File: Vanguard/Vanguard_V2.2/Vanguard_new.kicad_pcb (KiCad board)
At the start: 4 copper layers, 50 x 41.2 mm, 73 parts, among them J1 USB_C_Receptacle_USB2.0_16P, J2 Conn_02x03_Pin, J3 Micro_SD_Card_Det1, J4 STARBOARD_SERVO, J5 PORTSIDE_SERVO, J6 Conn_01x02_Pin, Q1 BSS138, Q2 BSS138, Q3 BSS138, Q4 BSS138, U1 ATSAMD11D14A-M, U2 ATmega4809-A, U3 AT25DF641A-SH-T, U4 AP2112K-3.3, U5 BD1020HFV, U6 BNO086, U7 TXB0104D, U8 TPS61092, U9 MPM3610AGQV-P, Y1 32.768kHz

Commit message: forgot a wire
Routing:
- net GND: track 152.7 -> 154.5 mm, vias 22 -> 23

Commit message: more wiring
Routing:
- net Net-(D1-GND): track 34.9 -> 44.5 mm, vias 2 -> 4
- net GND: track 154.5 -> 162.0 mm, vias 23 -> 25
- net Net-(D1-I/O1): track 22.6 -> 25.1 mm
- net Net-(PORTSIDE_RGB1-RA): track 0.00 -> 1.45 mm
- net Net-(D3-A): track 0.00 -> 0.83 mm

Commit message: some drc fixes not done
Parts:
- moved D6 0.66 mm to (528.0, 91.3)
- moved C4 0.40 mm to (526.0, 93.2)
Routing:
- net Net-(D1-GND): track 44.5 -> 45.6 mm
- net Net-(D6-K): track 21.9 -> 21.0 mm
- net GND: track 162.0 -> 161.5 mm

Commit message: Vangaurd 2.2. Done.
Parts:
- added ?: , clipboard:b9f70def-b1a4-4804-8b04-89d3a63594a6, F.Cu at (548.0, 88.5)
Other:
- board text added: "Portside"
- board text added: "Starboard"

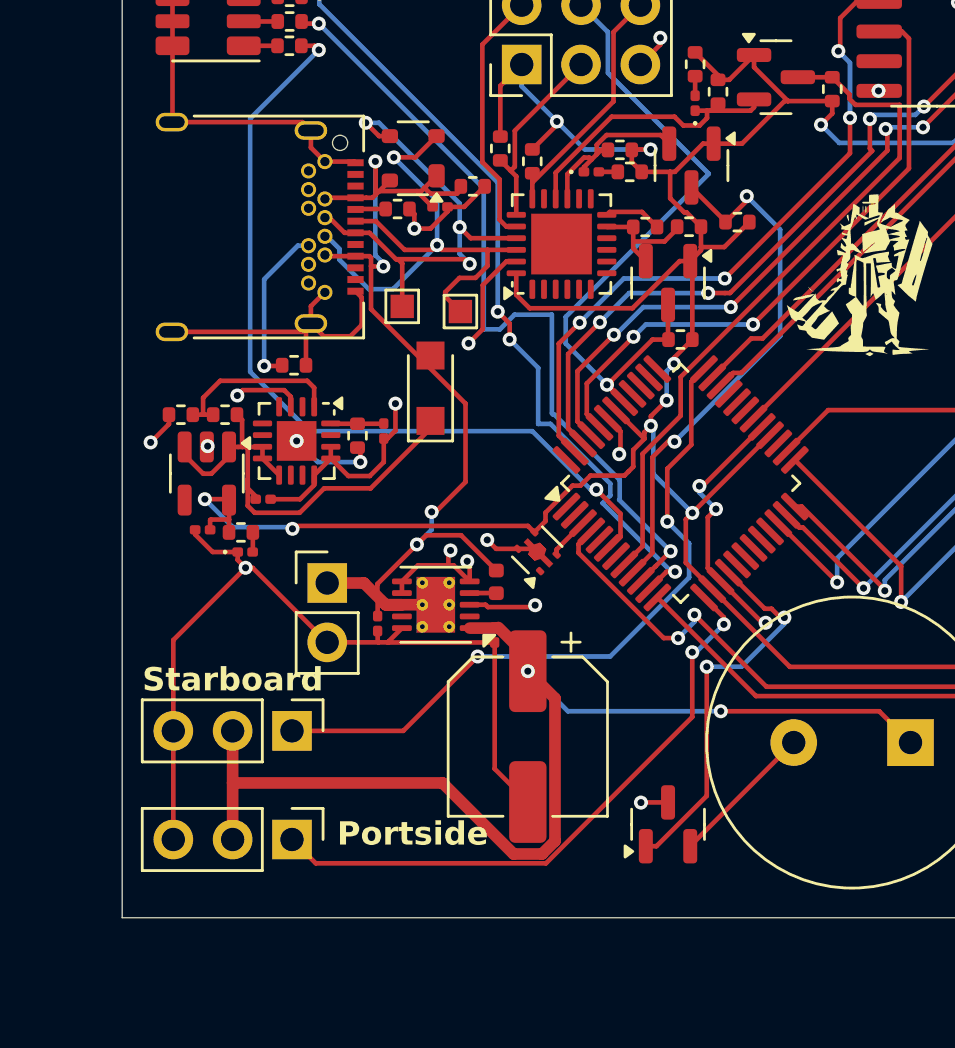
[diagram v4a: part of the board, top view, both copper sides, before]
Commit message: ejec servo added
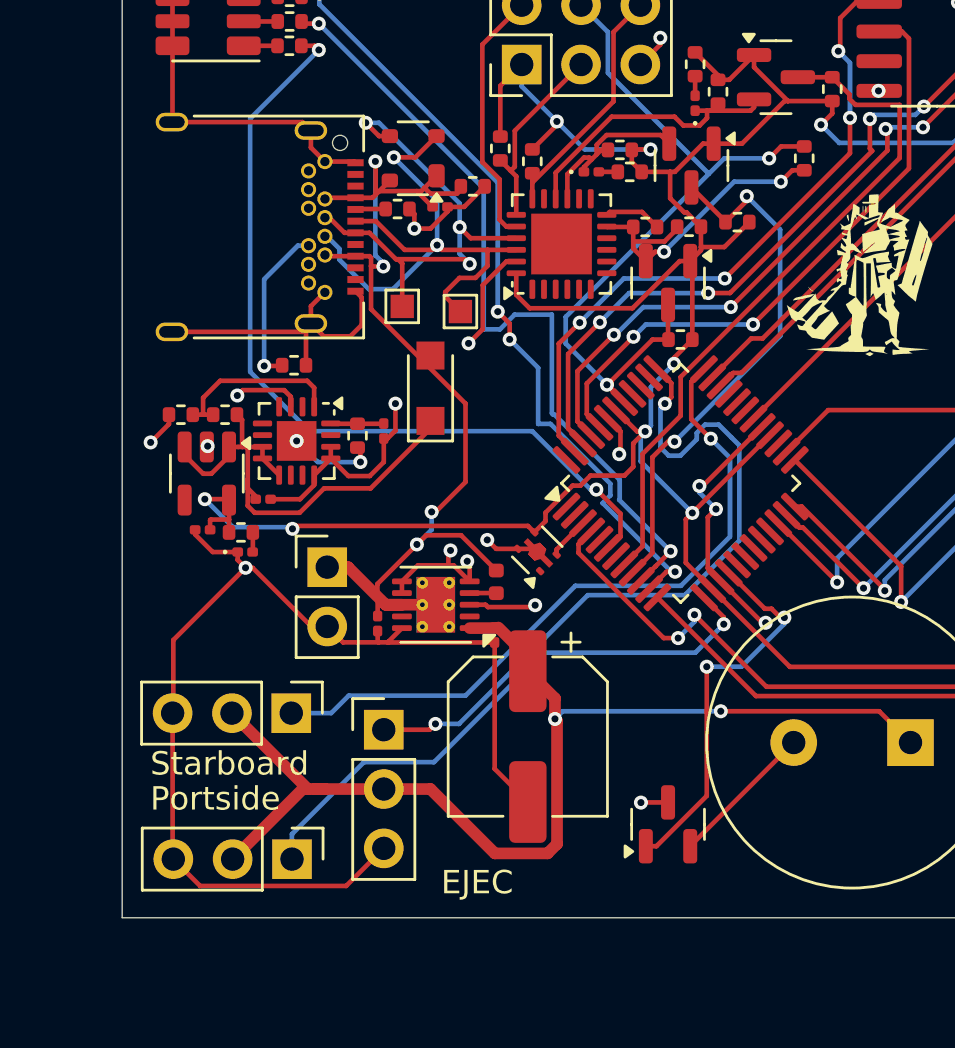
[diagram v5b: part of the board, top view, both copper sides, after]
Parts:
- added EJEC: EJECTION_SERVO, Connector_PinHeader_2.54mm:PinHeader_1x03_P2.54mm_Vertical, F.Cu at (526.0, 106.0)
- added R8: DNP, Resistor_SMD:R_0402_1005Metric, F.Cu at (544.0, 81.5)
- moved J5 0.84 mm to (522.1, 111.5)
- moved J4 0.76 mm to (522.0, 105.2)
- moved J6 0.68 mm to (523.6, 99.0)
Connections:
- U2 pad 37: unconnected-(U2-PF3-Pad37) -> EJEC_SERVO
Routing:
- net EJEC_SERVO: track 0.00 -> 31.0 mm, vias 0 -> 2
- net GND: track 161.5 -> 173.2 mm
- net /TX_UPDI: track 5.02 -> 13.4 mm, vias 0 -> 2
- net UPDI: track 28.6 -> 33.2 mm, vias 1 -> 2
- net PORT_SERVO: track 26.3 -> 24.8 mm, vias 2 -> 1
- net +5V: track 49.0 -> 49.7 mm
- net STAR_SERVO: track 29.7 -> 30.0 mm, vias 2 -> 1
- net +3.3V: track 176.1 -> 176.0 mm, vias 14 -> 13

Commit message: sd card rotato potato
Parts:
- moved ? 373.6 mm to (175.2, 112.4)
- moved J3 373.2 mm to (184.4, 112.7), turned to 90 degrees
- moved R23 373.1 mm to (190.2, 129.3)
- moved C2 373.1 mm to (185.2, 121.6)
- moved C5 373.1 mm to (148.3, 116.6)
- moved C7 373.1 mm to (185.1, 130.9)
- moved D2 373.1 mm to (162.3, 102.6)
- moved D3 373.1 mm to (166.8, 99.6)
- moved D5 373.1 mm to (147.5, 118.8)
- moved J5 373.1 mm to (149.5, 132.0)
- moved R13 373.1 mm to (172.7, 99.0)
- moved R15 373.1 mm to (146.7, 113.0)
- moved R16 373.1 mm to (144.8, 113.0)
- moved R18 373.1 mm to (186.1, 131.1)
- moved R20 373.1 mm to (189.3, 129.3)
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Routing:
- net GND: track 173.2 -> 161.0 mm
- net Net-(J3-CMD): track 7.72 -> 19.9 mm
- net Net-(J3-CLK): track 7.83 -> 18.4 mm
- net Net-(J3-DAT0): track 7.76 -> 17.4 mm
- net Net-(J3-DAT1): track 7.59 -> 17.0 mm
- net CD: track 8.80 -> 16.5 mm
- net +3.3V: track 176.0 -> 180.0 mm
- net D4: track 30.0 -> 28.8 mm

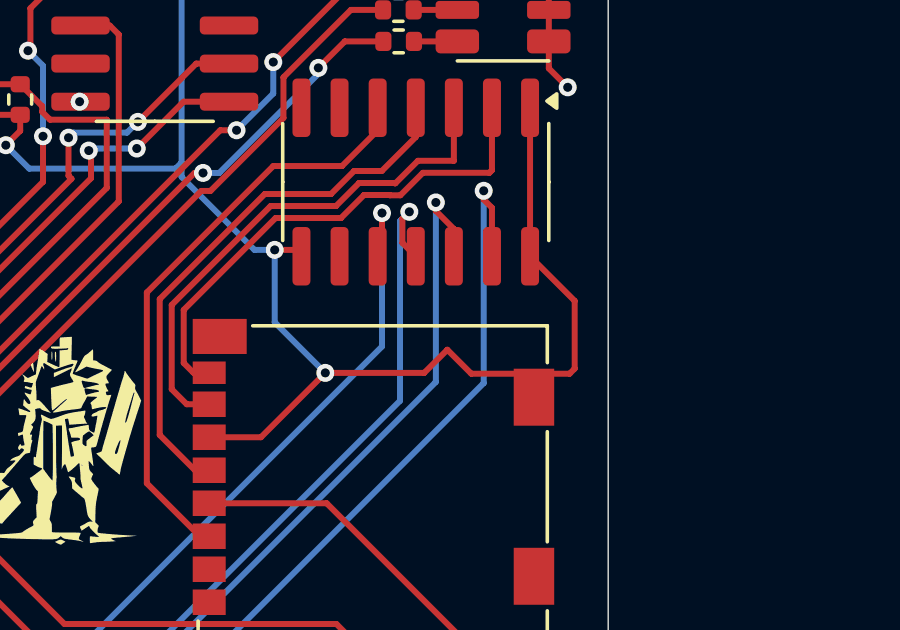
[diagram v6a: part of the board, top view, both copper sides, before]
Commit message: wire straight
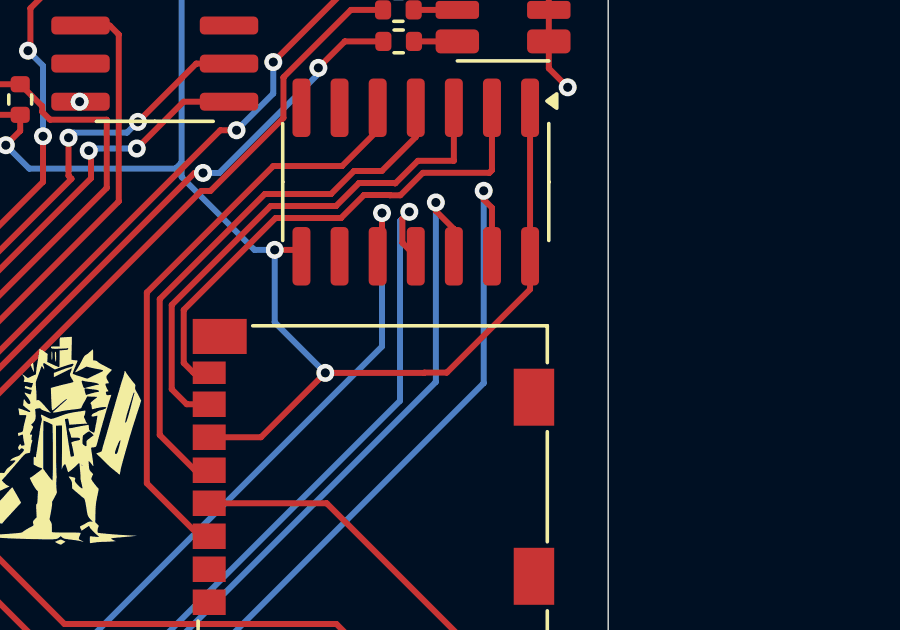
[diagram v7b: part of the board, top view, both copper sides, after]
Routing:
- net +3.3V: track 180.0 -> 175.7 mm
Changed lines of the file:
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@@
-	)
-	(segment
-		(start 187.6975 108.1575)
-		(end 190.9725 108.1575)
-		(width 0.2)
-		(layer "F.Cu")
-		(net 8)
 	)
 	(segment
@@
 	)
 	(segment
+		(start 186.135 108.12)
+		(end 186.88 108.12)
+		(width 0.2)
+		(layer "F.Cu")
+		(net 8)
+	)
+	(segment
 		(start 159.705614 108.3975)
 		(end 164.106948 108.3975)
@@
 	)
 	(segment
-		(start 186.125 108.13)
-		(end 182.83 108.13)
-		(width 0.2)
-		(layer "F.Cu")
-		(net 8)
-	)
-	(segment
 		(start 170.84802 123.75)
 		(end 179.71 123.75)
@@
 	)
 	(segment
+		(start 186.88 108.12)
+		(end 189.655 105.345)
+		(width 0.2)
+		(layer "F.Cu")
+		(net 8)
+	)
+	(segment
 		(start 186.0925 131.63)
 		(end 185.9625 131.76)
@@
 	)
 	(segment
-		(start 186.8975 107.3575)
+		(start 182.83 108.13)
 		(end 186.125 108.13)
 		(width 0.2)
@@
 	)
 	(segment
+		(start 186.125 108.13)
+		(end 186.135 108.12)
+		(width 0.2)
+		(layer "F.Cu")
+		(net 8)
+	)
+	(segment
 		(start 167.77 98.6175)
 		(end 168.25 98.6175)
@@
 	)
 	(segment
-		(start 190.9725 108.1575)
-		(end 191.1425 107.9875)
-		(width 0.2)
-		(layer "F.Cu")
-		(net 8)
-	)
-	(segment
 		(start 166.668883 117.158883)
 		(end 166.39 117.437766)
@@
 	)
 	(segment
+		(start 189.655 105.345)
+		(end 189.655 104.2425)
+		(width 0.2)
+		(layer "F.Cu")
+		(net 8)
+	)
+	(segment
 		(start 146.025 117.4725)
 		(end 146.055 117.4425)
@@
 	)
 	(segment
-		(start 191.1425 105.73)
-		(end 189.655 104.2425)
-		(width 0.2)
-		(layer "F.Cu")
-		(net 8)
-	)
-	(segment
 		(start 172.66 99.5275)
 		(end 170.763052 99.5275)
@@
 	)
 	(segment
-		(start 191.1425 107.9875)
-		(end 191.1425 105.73)
-		(width 0.2)
-		(layer "F.Cu")
-		(net 8)
-	)
-	(segment
 		(start 167.04 105.9175)
 		(end 166.58 106.3775)
@@
 		(width 0.2)
 		(layer "F.Cu")
-		(net 8)
-	)
-	(segment
-		(start 186.8975 107.3575)
-		(end 187.6975 108.1575)
-		(width 0.2)
-		(layer "F.Cu")

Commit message: vias
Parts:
- moved C1 0.16 mm to (155.9, 104.2)
- moved ? 0.15 mm to (175.2, 112.2)
- moved C3 0.08 mm to (184.5, 121.5)
- moved C2 0.08 mm to (185.2, 121.5)
- moved Y1 0.08 mm to (185.7, 123.9)
- moved L1 0.07 mm to (158.3, 120.1)
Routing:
- net GND: track 161.0 -> 164.4 mm, vias 25 -> 36
- net D7: track 34.3 -> 32.7 mm
- net D6: track 30.3 -> 29.1 mm
- net PA0/MISO: track 26.7 -> 27.7 mm
- net PORT_RED: track 24.3 -> 25.1 mm
- net Net-(J3-DAT0): track 17.4 -> 16.7 mm
- net PORT_BLUE: track 24.6 -> 25.2 mm
- net PORT_GREEN: track 23.1 -> 23.6 mm
